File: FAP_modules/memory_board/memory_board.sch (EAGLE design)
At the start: 29 parts, among them IC1 74HC32, IC2 74HC04, IC4 74HC245DW, IC5 AT28C256

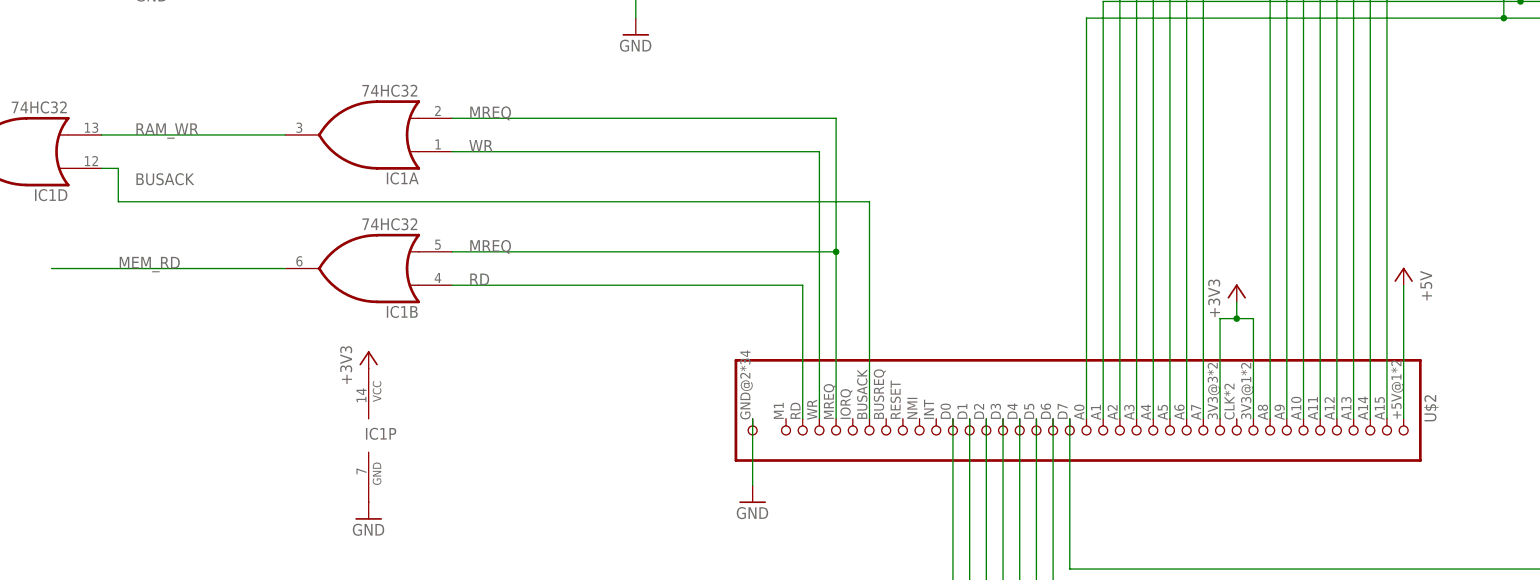
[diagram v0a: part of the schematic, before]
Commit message: added interrupt chaining and WAIT
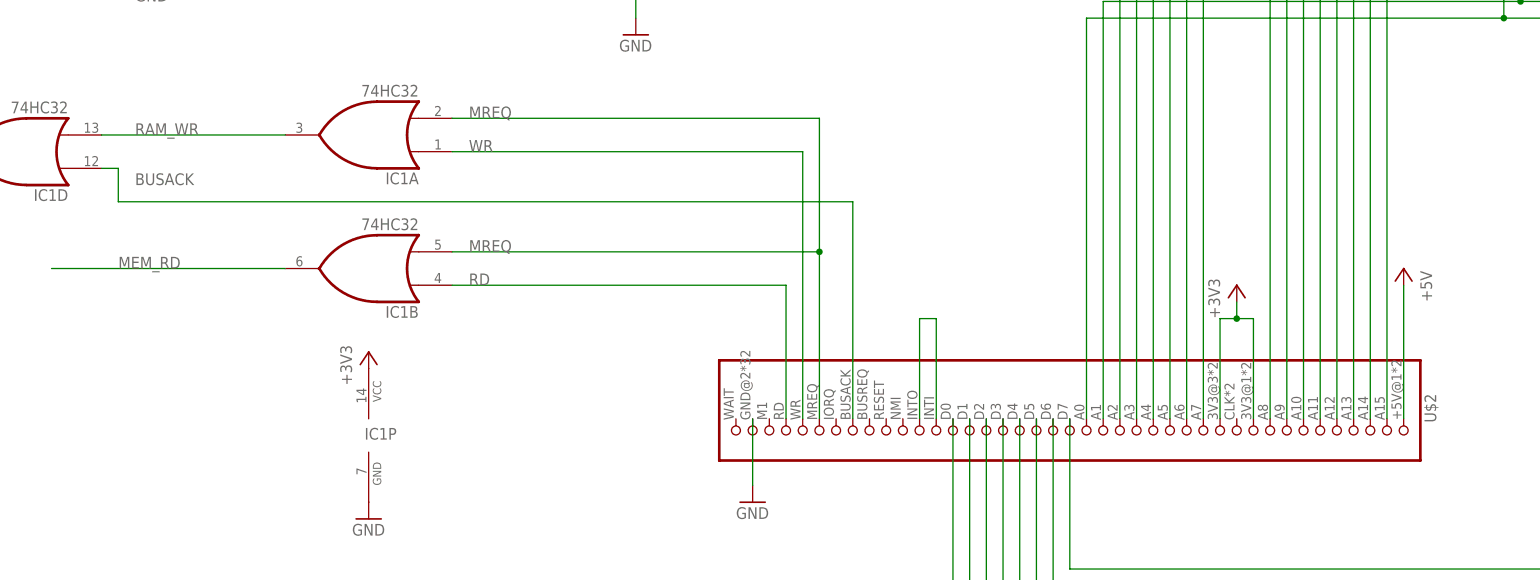
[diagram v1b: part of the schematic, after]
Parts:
- U$2: value FAP_BUS -> FAP_BUS_FAP_BUS; device fap_bus:FAP_BUS -> cpu_board:FAP_BUS_FAP_BUS
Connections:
- new net N$33: U$2.29, U$2.39
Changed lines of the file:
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@@
 <?xml version="1.0" encoding="utf-8"?>
 <!DOCTYPE eagle SYSTEM "eagle.dtd">
-<eagle version="7.6.0">
+<eagle version="7.7.0">
 <drawing>
 <settings>
@@
 <part name="IC3" library="memory-hitachi" deviceset="62256P" device=""/>
 <part name="IC2" library="74xx-us" deviceset="74*04" device="D" technology="LS" value="74HC04"/>
-<part name="U$2" library="fap_bus" deviceset="FAP_BUS" device=""/>
+<part name="U$2" library="cpu_board" deviceset="FAP_BUS_FAP_BUS" device=""/>
 <part name="IC4" library="74xx-eu" deviceset="74*245" device="DW" technology="HC"/>
 <part name="GND1" library="supply1" deviceset="GND" device=""/>
@@
 <pinref part="U$2" gate="G$1" pin="35"/>
 <pinref part="IC1" gate="A" pin="I1"/>
-<wire x1="96.52" y1="-25.4" x2="96.52" y2="0" width="0.1524" layer="91"/>
-<wire x1="96.52" y1="0" x2="96.52" y2="20.32" width="0.1524" layer="91"/>
-<wire x1="96.52" y1="20.32" x2="38.1" y2="20.32" width="0.1524" layer="91"/>
+<wire x1="93.98" y1="-25.4" x2="93.98" y2="0" width="0.1524" layer="91"/>
+<wire x1="93.98" y1="0" x2="93.98" y2="20.32" width="0.1524" layer="91"/>
+<wire x1="93.98" y1="20.32" x2="38.1" y2="20.32" width="0.1524" layer="91"/>
 <pinref part="IC1" gate="B" pin="I1"/>
-<wire x1="96.52" y1="0" x2="38.1" y2="0" width="0.1524" layer="91"/>
-<junction x="96.52" y="0"/>
+<wire x1="93.98" y1="0" x2="38.1" y2="0" width="0.1524" layer="91"/>
+<junction x="93.98" y="0"/>
 <label x="40.64" y="0" size="1.778" layer="95"/>
 <label x="40.64" y="20.32" size="1.778" layer="95"/>
@@
 <pinref part="U$2" gate="G$1" pin="36"/>
 <pinref part="IC1" gate="A" pin="I0"/>
-<wire x1="93.98" y1="-25.4" x2="93.98" y2="15.24" width="0.1524" layer="91"/>
-<wire x1="93.98" y1="15.24" x2="38.1" y2="15.24" width="0.1524" layer="91"/>
+<wire x1="91.44" y1="-25.4" x2="91.44" y2="15.24" width="0.1524" layer="91"/>
+<wire x1="91.44" y1="15.24" x2="38.1" y2="15.24" width="0.1524" layer="91"/>
 <label x="40.64" y="15.24" size="1.778" layer="95"/>
 </segment>
@@
 <pinref part="U$2" gate="G$1" pin="37"/>
 <pinref part="IC1" gate="B" pin="I0"/>
-<wire x1="91.44" y1="-25.4" x2="91.44" y2="-5.08" width="0.1524" layer="91"/>
-<wire x1="91.44" y1="-5.08" x2="38.1" y2="-5.08" width="0.1524" layer="91"/>
+<wire x1="88.9" y1="-25.4" x2="88.9" y2="-5.08" width="0.1524" layer="91"/>
+<wire x1="88.9" y1="-5.08" x2="38.1" y2="-5.08" width="0.1524" layer="91"/>
 <label x="40.64" y="-5.08" size="1.778" layer="95"/>
 </segment>
@@
 <segment>
 <pinref part="U$2" gate="G$1" pin="33"/>
-<wire x1="101.6" y1="-25.4" x2="101.6" y2="7.62" width="0.1524" layer="91"/>
+<wire x1="99.06" y1="-25.4" x2="99.06" y2="7.62" width="0.1524" layer="91"/>
 <label x="-10.16" y="10.16" size="1.778" layer="95"/>
-<wire x1="101.6" y1="7.62" x2="-12.7" y2="7.62" width="0.1524" layer="91"/>
+<wire x1="99.06" y1="7.62" x2="-12.7" y2="7.62" width="0.1524" layer="91"/>
 <wire x1="-12.7" y1="7.62" x2="-12.7" y2="12.7" width="0.1524" layer="91"/>
 <wire x1="-12.7" y1="12.7" x2="-15.24" y2="12.7" width="0.1524" layer="91"/>
@@
 </segment>
 </net>
+<net name="N$33" class="0">
+<segment>
+<pinref part="U$2" gate="G$1" pin="39"/>
+<wire x1="109.22" y1="-25.4" x2="109.22" y2="-10.16" width="0.1524" layer="91"/>
+<pinref part="U$2" gate="G$1" pin="29"/>
+<wire x1="109.22" y1="-10.16" x2="111.76" y2="-10.16" width="0.1524" layer="91"/>
+<wire x1="111.76" y1="-10.16" x2="111.76" y2="-25.4" width="0.1524" layer="91"/>
+</segment>
+</net>

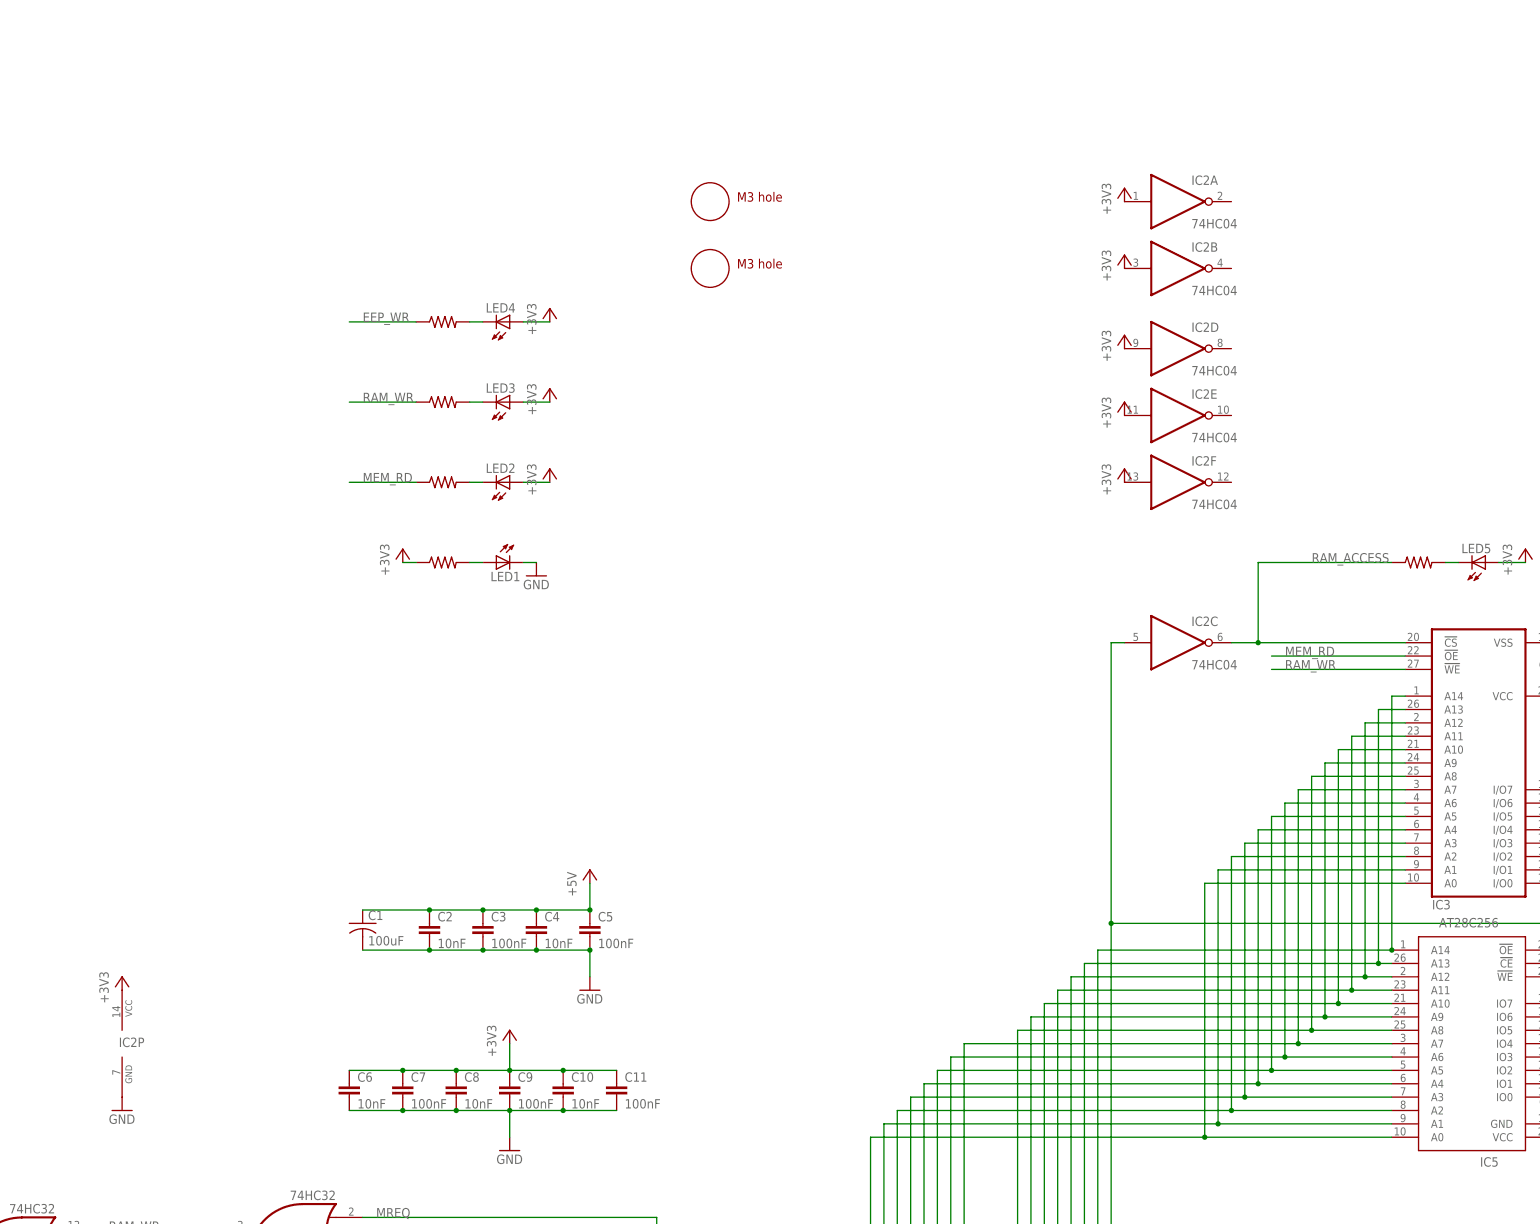
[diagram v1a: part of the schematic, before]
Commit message: new memory board
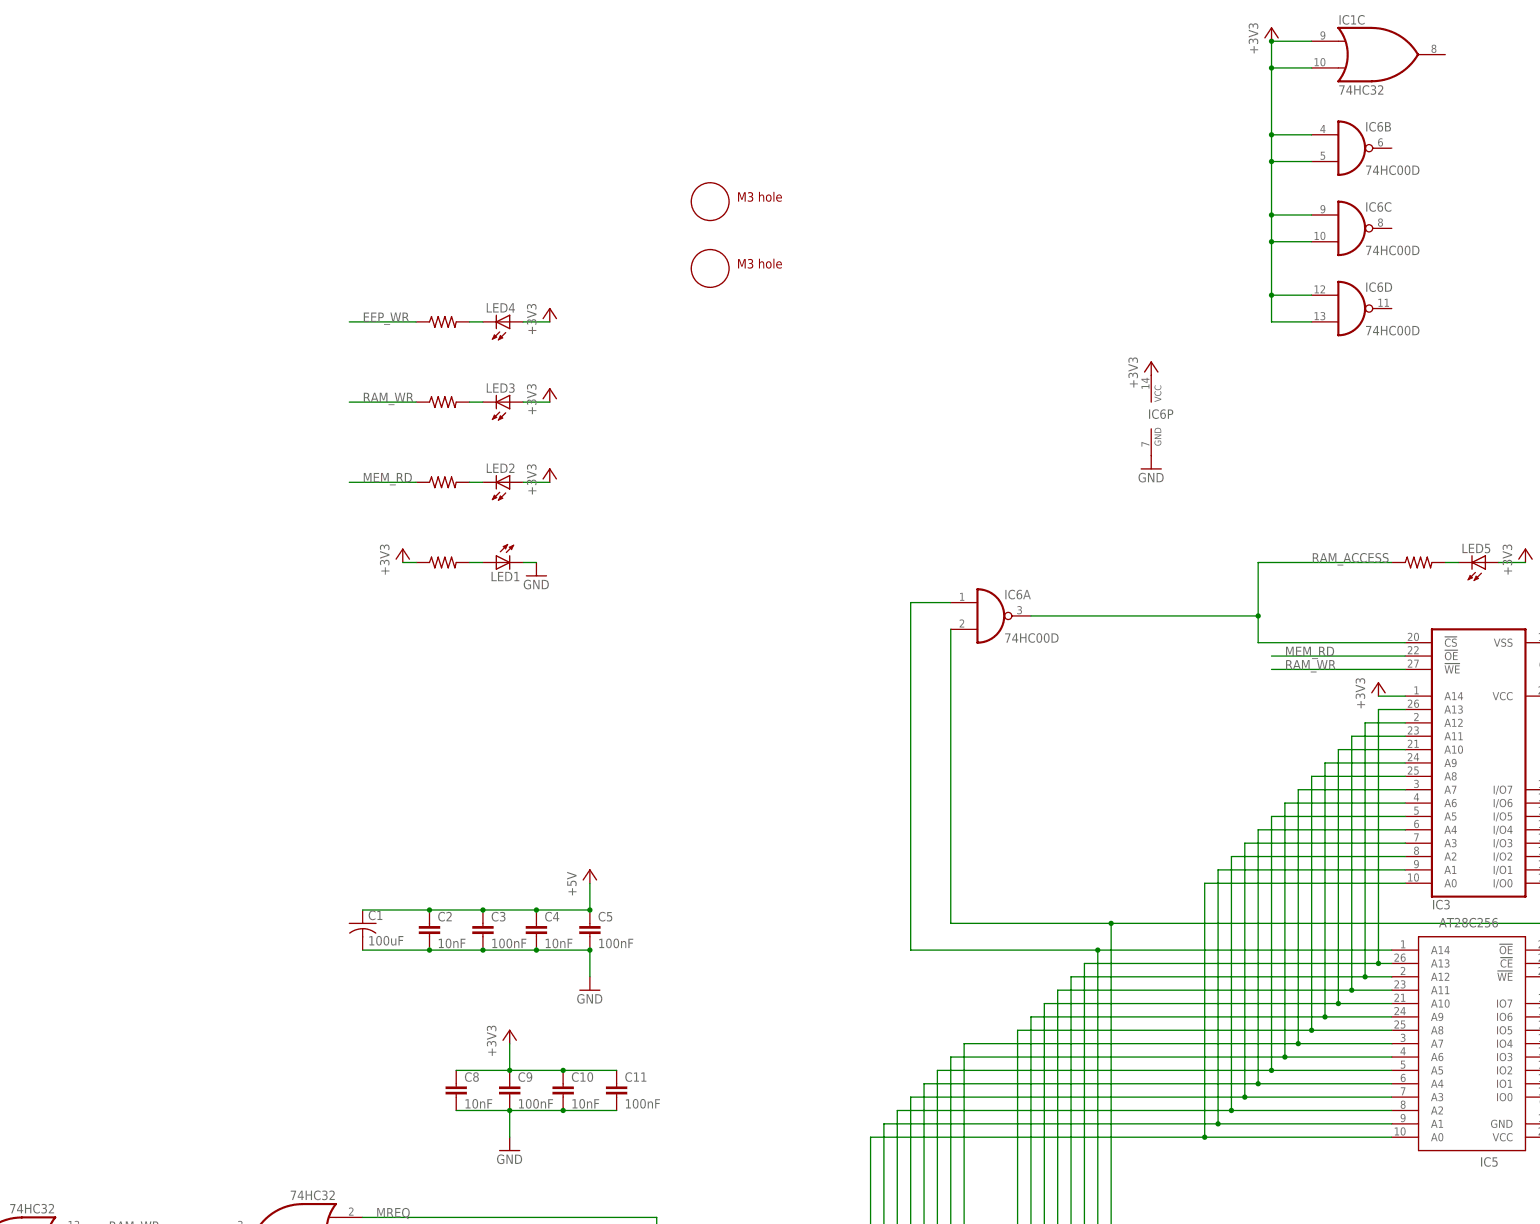
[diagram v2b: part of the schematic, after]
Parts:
- removed C6: 10nF, SparkFun-Capacitors:22UF-6.3V-20%(0805)
- removed C7: 100nF, SparkFun-Capacitors:22UF-6.3V-20%(0805)
- removed IC2: 74HC04, 74xx-us:74LS04D
- added IC6: 74HC00D, 74xx-eu:74HC00D
- R1, R2, R3, R7, R8: value 50 -> 2K
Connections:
- net +3V3: now also IC1C.I0, IC1C.I1, IC3.A14, IC6B.I0, IC6B.I1, IC6C.I0, IC6C.I1, IC6D.I0, IC6D.I1, IC6P.VCC; no longer C6.1, C7.1, IC2A.I, IC2B.I, IC2D.I, IC2E.I, IC2F.I, IC2P.VCC
- net GND: now also IC6P.GND; no longer C6.2, C7.2, IC2P.GND
- net N$32: now also IC6A.I1; no longer IC2C.I
- net N$9: now also IC6A.I0; no longer IC3.A14
- net RAM_ACCESS: now also IC6A.O; no longer IC2C.O

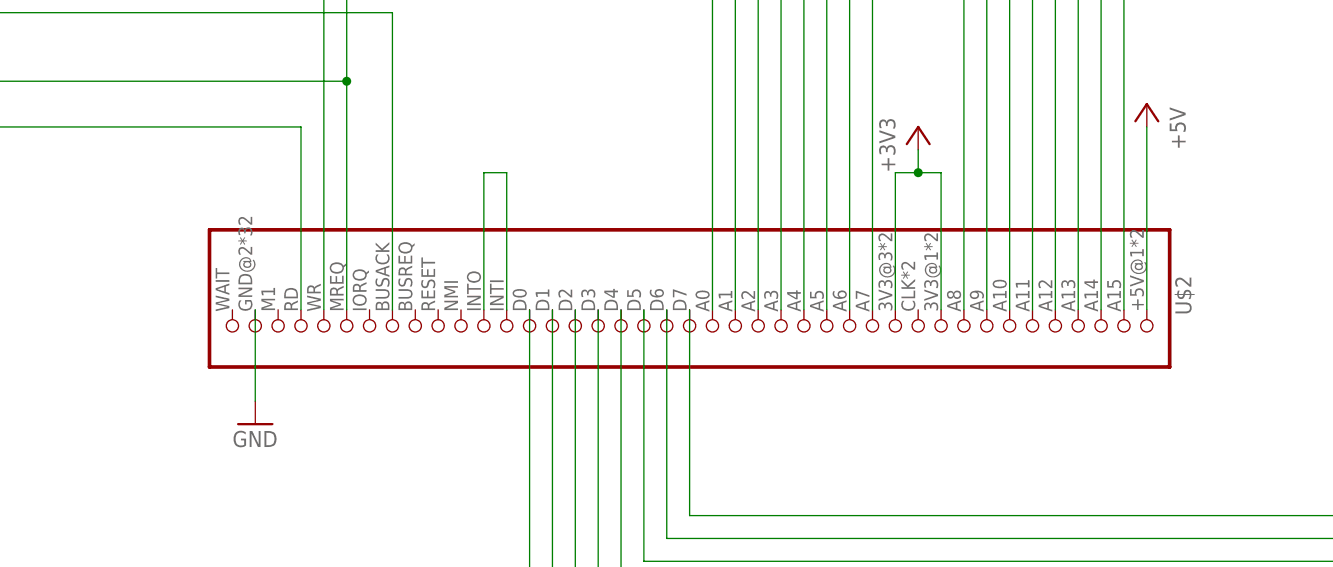
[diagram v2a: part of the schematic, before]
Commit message: added all Z80 signals on bus
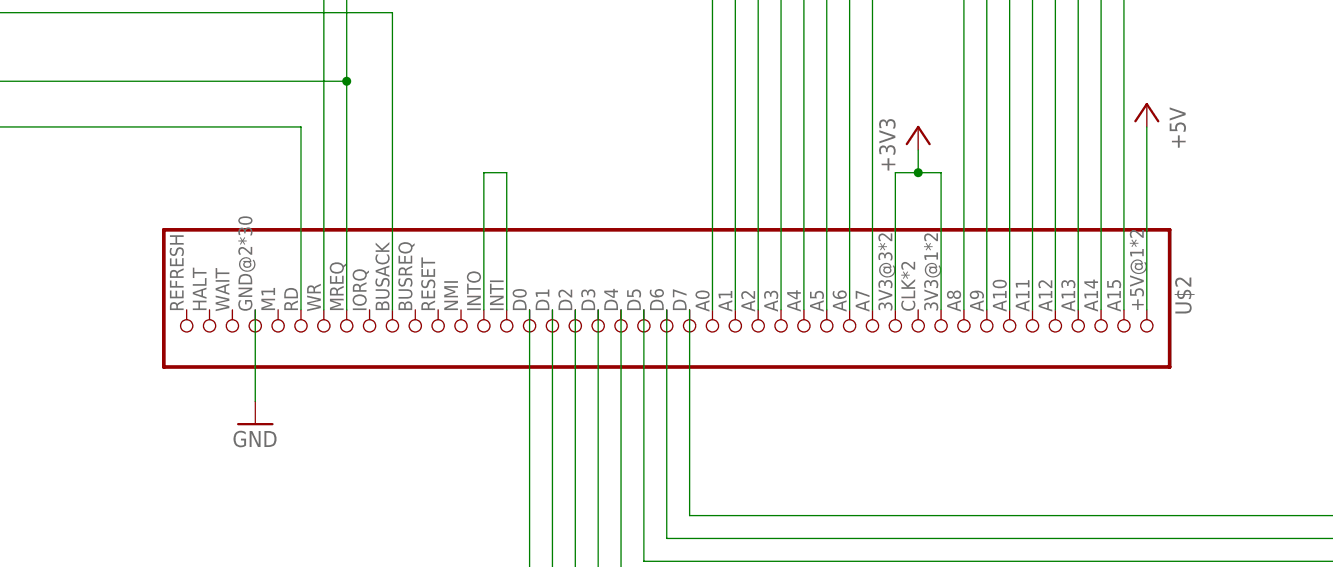
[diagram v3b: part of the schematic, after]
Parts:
- U$2: value FAP_BUS_FAP_BUS -> FAP_BUS; device cpu_board:FAP_BUS_FAP_BUS -> fap_bus:FAP_BUS
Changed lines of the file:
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@@
 <part name="IC1" library="74xx-us" deviceset="74*32" device="D" technology="S" value="74HC32"/>
 <part name="IC3" library="memory-hitachi" deviceset="62256P" device=""/>
-<part name="U$2" library="cpu_board" deviceset="FAP_BUS_FAP_BUS" device=""/>
+<part name="U$2" library="fap_bus" deviceset="FAP_BUS" device=""/>
 <part name="IC4" library="74xx-eu" deviceset="74*245" device="DW" technology="HC"/>
 <part name="GND1" library="supply1" deviceset="GND" device=""/>
